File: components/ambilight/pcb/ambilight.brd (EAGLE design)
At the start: 69.2 x 54.7 mm, 12 parts, among them IC1 7805T

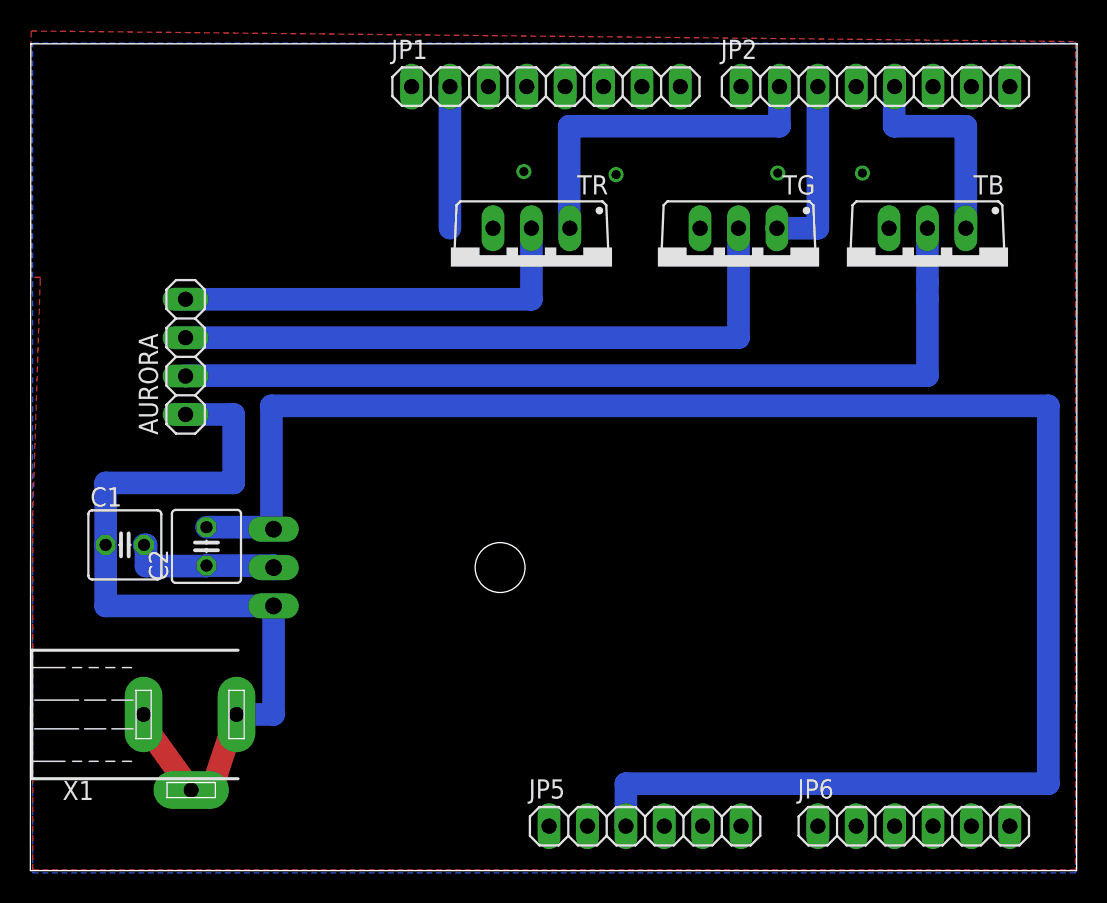
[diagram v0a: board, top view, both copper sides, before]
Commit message: Added Socket PCB, fixed ambilight sketch a bit
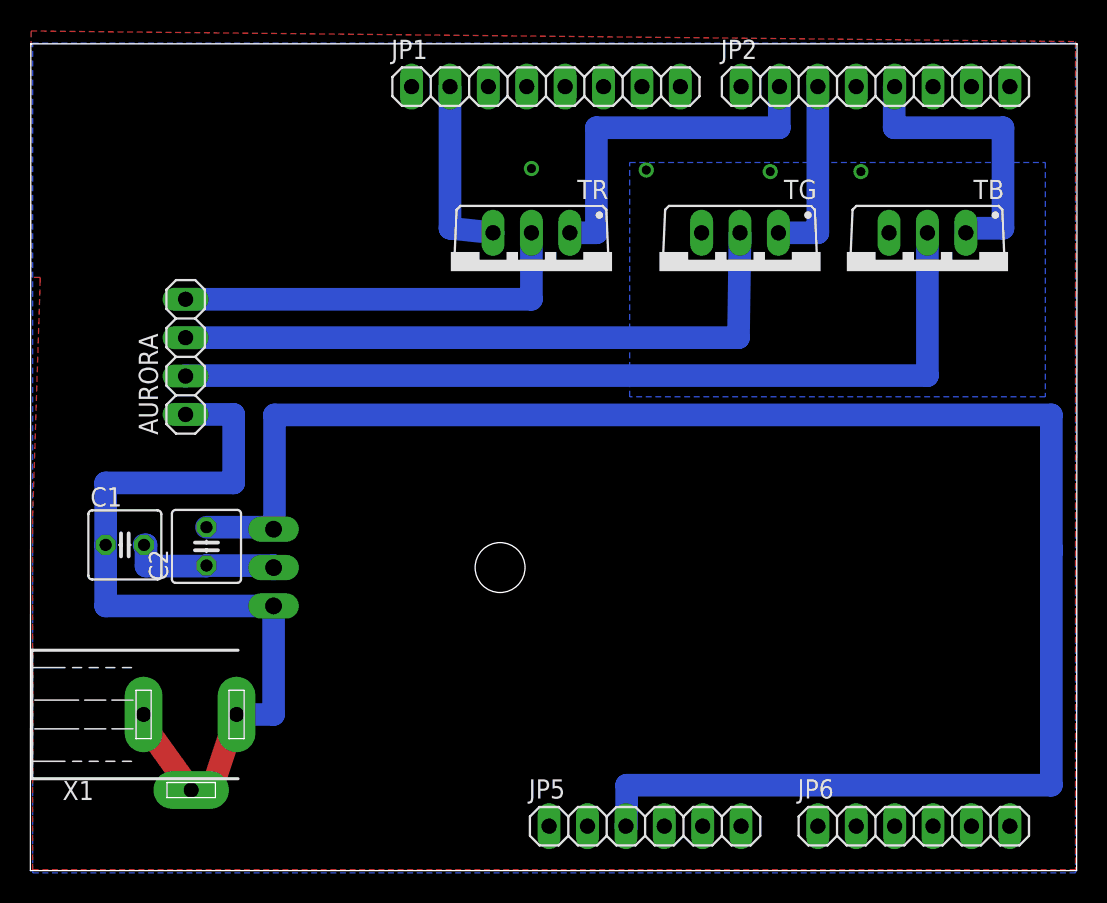
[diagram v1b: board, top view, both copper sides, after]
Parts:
- moved TG 0.32 mm to (77.4, 45.9)
- moved TB 0.30 mm to (89.8, 45.9)
- moved TR 0.30 mm to (63.6, 45.9)
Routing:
- net N$7: track 14.1 -> 19.4 mm
- net GND: track 25.3 -> 28.1 mm, vias 2 -> 4
- net N$4: track 120.0 -> 119.1 mm
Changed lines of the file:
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@@
 </autorouter>
 <elements>
-<element name="TR" library="transistor-power" package="TO220BV" value="foo" x="63.6" y="46.21" rot="R180"/>
-<element name="TG" library="transistor-power" package="TO220BV" value="foo" x="77.3" y="46.21" rot="R180"/>
-<element name="TB" library="transistor-power" package="TO220BV" value="foo" x="89.8" y="46.21" rot="R180"/>
+<element name="TR" library="transistor-power" package="TO220BV" value="foo" x="63.6" y="45.91" rot="R180"/>
+<element name="TG" library="transistor-power" package="TO220BV" value="foo" x="77.4" y="45.91" rot="R180"/>
+<element name="TB" library="transistor-power" package="TO220BV" value="foo" x="89.8" y="45.91" rot="R180"/>
 <element name="X1" library="con-conrad" package="733980-62" value="" x="35.52" y="16.58" rot="R270"/>
 <element name="AURORA" library="pinhead" package="1X04" value="" x="40.72" y="40.24" rot="R90"/>
@@
 <vertex x="30.5" y="61.8"/>
 </polygon>
-<via x="79.9" y="52.4" extent="1-16" drill="0.6" shape="square"/>
 <contactref element="JP1" pad="2"/>
-<wire x1="58.21" y1="48.75" x2="58.21" y2="58.12" width="1.5" layer="16"/>
-<via x="85.5" y="52.4" extent="1-16" drill="0.6" shape="square"/>
 <contactref element="X1" pad="2"/>
 <contactref element="X1" pad="3"/>
@@
 <wire x1="38.1" y1="26.4" x2="42.1" y2="26.4" width="1.5" layer="16"/>
 <wire x1="42.1" y1="26.4" x2="42.1" y2="26.43" width="1.5" layer="16"/>
+<wire x1="61.06" y1="48.45" x2="58.21" y2="48.75" width="1.5" layer="16"/>
+<wire x1="58.21" y1="48.75" x2="58.21" y2="58.12" width="1.5" layer="16"/>
+<polygon width="1.5" layer="16" spacing="1.2" isolate="0.8">
+<vertex x="70.1" y="53.1"/>
+<vertex x="97.6" y="53.1"/>
+<vertex x="97.6" y="37.6"/>
+<vertex x="70.1" y="37.6"/>
+</polygon>
+<via x="63.6" y="52.7" extent="1-16" drill="0.6"/>
+<via x="71.2" y="52.6" extent="1-16" drill="0.6"/>
+<via x="79.4" y="52.5" extent="1-16" drill="0.6"/>
+<via x="85.4" y="52.5" extent="1-16" drill="0.6"/>
 </signal>
 <signal name="N$4">
@@
 <contactref element="IC1" pad="3"/>
 <contactref element="C2" pad="2"/>
-<wire x1="46.54" y1="28.84" x2="46.4" y2="28.84" width="1.5" layer="16"/>
-<wire x1="46.4" y1="28.84" x2="46.4" y2="37" width="1.5" layer="16"/>
-<wire x1="46.4" y1="37" x2="97.8" y2="37" width="1.5" layer="16"/>
-<wire x1="97.8" y1="37" x2="97.8" y2="12" width="1.5" layer="16"/>
-<wire x1="97.8" y1="12" x2="69.85" y2="12" width="1.5" layer="16"/>
-<wire x1="69.85" y1="12" x2="69.85" y2="9.19" width="1.5" layer="16"/>
 <wire x1="42.1" y1="28.97" x2="46.54" y2="28.97" width="1.5" layer="16"/>
 <wire x1="46.54" y1="28.97" x2="46.54" y2="28.84" width="1.5" layer="16"/>
+<wire x1="46.54" y1="28.84" x2="46.4" y2="28.84" width="1.5" layer="16"/>
+<wire x1="46.54" y1="28.84" x2="46.6" y2="28.84" width="1.5" layer="16"/>
+<wire x1="46.6" y1="28.84" x2="46.6" y2="36.4" width="1.5" layer="16"/>
+<wire x1="46.6" y1="36.4" x2="98" y2="36.4" width="1.5" layer="16"/>
+<wire x1="98" y1="36.4" x2="98" y2="27.6" width="1.5" layer="16"/>
+<wire x1="98" y1="27.6" x2="98" y2="27.3" width="1.5" layer="16"/>
+<wire x1="69.85" y1="9.19" x2="69.9" y2="9.19" width="1.5" layer="16"/>
+<wire x1="69.9" y1="9.19" x2="69.9" y2="11.9" width="1.5" layer="16"/>
+<wire x1="69.9" y1="11.9" x2="98" y2="11.9" width="1.5" layer="16"/>
+<wire x1="98" y1="11.9" x2="98" y2="27.3" width="1.5" layer="16"/>
 </signal>
 <signal name="N$7">
@@
 <contactref element="JP2" pad="5"/>
 <wire x1="87.63" y1="58.12" x2="87.6" y2="58.12" width="1.5" layer="16"/>
-<wire x1="87.6" y1="58.12" x2="87.6" y2="55.5" width="1.5" layer="16"/>
-<wire x1="87.6" y1="55.5" x2="92.34" y2="55.5" width="1.5" layer="16"/>
-<wire x1="92.34" y1="55.5" x2="92.34" y2="48.75" width="1.5" layer="16"/>
+<wire x1="87.6" y1="58.12" x2="87.6" y2="55.4" width="1.5" layer="16"/>
+<wire x1="92.34" y1="48.45" x2="92.3" y2="48.75" width="1.5" layer="16"/>
+<wire x1="87.6" y1="55.4" x2="94.8" y2="55.4" width="1.5" layer="16"/>
+<wire x1="92.3" y1="48.75" x2="94.8" y2="48.75" width="1.5" layer="16"/>
+<wire x1="94.8" y1="48.75" x2="94.8" y2="55.4" width="1.5" layer="16"/>
 </signal>
 <signal name="N$9">
 <contactref element="TG" pad="G"/>
 <contactref element="JP2" pad="3"/>
-<wire x1="79.84" y1="48.75" x2="82.55" y2="48.75" width="1.5" layer="16"/>
-<wire x1="82.55" y1="48.75" x2="82.55" y2="58.12" width="1.5" layer="16"/>
+<wire x1="79.94" y1="48.45" x2="82.55" y2="48.45" width="1.5" layer="16"/>
+<wire x1="82.55" y1="48.45" x2="82.55" y2="58.12" width="1.5" layer="16"/>
 </signal>
 <signal name="N$10">
 <contactref element="TR" pad="G"/>
 <contactref element="JP2" pad="2"/>
-<wire x1="66.14" y1="48.75" x2="66.1" y2="48.75" width="1.5" layer="16"/>
-<wire x1="66.1" y1="48.75" x2="66.1" y2="55.5" width="1.5" layer="16"/>
-<wire x1="66.1" y1="55.5" x2="80.01" y2="55.5" width="1.5" layer="16"/>
-<wire x1="80.01" y1="55.5" x2="80.01" y2="58.12" width="1.5" layer="16"/>
+<wire x1="80.01" y1="58.12" x2="80" y2="58.12" width="1.5" layer="16"/>
+<wire x1="80" y1="58.12" x2="80" y2="55.4" width="1.5" layer="16"/>
+<wire x1="66.14" y1="48.45" x2="67.9" y2="48.45" width="1.5" layer="16"/>
+<wire x1="67.9" y1="48.45" x2="67.9" y2="55.4" width="1.5" layer="16"/>
+<wire x1="67.9" y1="55.4" x2="80" y2="55.4" width="1.5" layer="16"/>
 </signal>
 <signal name="N$11">
@@
 <contactref element="AURORA" pad="4"/>
 <wire x1="40.72" y1="44.05" x2="63.6" y2="44.05" width="1.5" layer="16"/>
-<wire x1="63.6" y1="44.05" x2="63.6" y2="48.75" width="1.5" layer="16"/>
+<wire x1="63.6" y1="44.05" x2="63.6" y2="48.45" width="1.5" layer="16"/>
 </signal>
 <signal name="N$12">
@@
 <contactref element="AURORA" pad="3"/>
 <wire x1="40.72" y1="41.51" x2="77.3" y2="41.51" width="1.5" layer="16"/>
-<wire x1="77.3" y1="41.51" x2="77.3" y2="48.75" width="1.5" layer="16"/>
+<wire x1="77.3" y1="41.51" x2="77.4" y2="48.45" width="1.5" layer="16"/>
 </signal>
 <signal name="N$13">
 <contactref element="TB" pad="D"/>
 <contactref element="AURORA" pad="2"/>
-<wire x1="89.8" y1="48.75" x2="89.8" y2="45.2" width="1.5" layer="16"/>
-<wire x1="89.8" y1="45.2" x2="89.8" y2="44.1" width="1.5" layer="16"/>
 <wire x1="89.8" y1="39" x2="40.72" y2="39" width="1.5" layer="16"/>
 <wire x1="40.72" y1="39" x2="40.72" y2="38.97" width="1.5" layer="16"/>
-<wire x1="89.8" y1="39" x2="89.8" y2="44.1" width="1.5" layer="16"/>
+<wire x1="89.8" y1="39" x2="89.8" y2="48.45" width="1.5" layer="16"/>
 </signal>
 <signal name="N$16">
@@
 </signal>
 <signal name="S$1">
-<via x="69.2" y="52.3" extent="1-16" drill="0.6" shape="square"/>
 </signal>
 <signal name="S$2">
-<via x="63.1" y="52.5" extent="1-16" drill="0.6" shape="square"/>
 </signal>
 </signals>

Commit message: Worked on pcbs
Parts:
- C1: device rcl:C025-050X050 -> resistor:C050-025X075
- moved C1 1.84 mm to (38.1, 29.0), turned to 270 degrees
- moved X1 0.22 mm to (35.7, 16.7)
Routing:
- net GND: track 28.1 -> 22.6 mm
- net S$3: track 0.00 -> 4.30 mm
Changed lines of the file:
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@@
 <element name="TG" library="transistor-power" package="TO220BV" value="foo" x="77.4" y="45.91" rot="R180"/>
 <element name="TB" library="transistor-power" package="TO220BV" value="foo" x="89.8" y="45.91" rot="R180"/>
-<element name="X1" library="con-conrad" package="733980-62" value="" x="35.52" y="16.58" rot="R270"/>
+<element name="X1" library="con-conrad" package="733980-62" value="" x="35.72" y="16.68" rot="R270"/>
 <element name="AURORA" library="pinhead" package="1X04" value="" x="40.72" y="40.24" rot="R90"/>
 <element name="JP1" library="pinhead" package="1X08" value="" x="64.56" y="58.12"/>
@@
 <element name="JP6" library="pinhead" package="1X06" value="" x="88.9" y="9.19"/>
 <element name="IC1" library="linear" package="TO220H" value="7805T" x="56.7" y="26.3" rot="MR90"/>
-<element name="C1" library="rcl" package="C025-050X050" value="330n" x="36.7" y="27.8"/>
+<element name="C1" library="resistor" package="C050-025X075" value="330n" x="38.1" y="29" rot="R270"/>
 <element name="C2" library="rcl" package="C025-050X050" value="100n" x="42.1" y="27.7" rot="R90"/>
 </elements>
@@
 <contactref element="C1" pad="2"/>
 <contactref element="C2" pad="1"/>
-<wire x1="41.09" y1="11.58" x2="37.78" y2="16.18" width="1.5" layer="1"/>
+<wire x1="41.29" y1="11.68" x2="37.78" y2="16.18" width="1.5" layer="1"/>
 <wire x1="46.54" y1="26.2" x2="46.54" y2="26.3" width="1.5" layer="16"/>
 <wire x1="42.1" y1="26.43" x2="46.54" y2="26.43" width="1.5" layer="16"/>
 <wire x1="46.54" y1="26.43" x2="46.54" y2="26.3" width="1.5" layer="16"/>
-<wire x1="37.97" y1="27.8" x2="38.1" y2="27.8" width="1.5" layer="16"/>
-<wire x1="38.1" y1="27.8" x2="38.1" y2="26.4" width="1.5" layer="16"/>
-<wire x1="38.1" y1="26.4" x2="42.1" y2="26.4" width="1.5" layer="16"/>
-<wire x1="42.1" y1="26.4" x2="42.1" y2="26.43" width="1.5" layer="16"/>
 <wire x1="61.06" y1="48.45" x2="58.21" y2="48.75" width="1.5" layer="16"/>
 <wire x1="58.21" y1="48.75" x2="58.21" y2="58.12" width="1.5" layer="16"/>
@@
 <contactref element="IC1" pad="1"/>
 <contactref element="C1" pad="1"/>
-<wire x1="44.09" y1="16.58" x2="42.3" y2="11.18" width="1.5" layer="1"/>
-<wire x1="44.09" y1="16.58" x2="46.54" y2="16.58" width="1.5" layer="16"/>
+<wire x1="44.29" y1="16.68" x2="42.3" y2="11.18" width="1.5" layer="1"/>
+<wire x1="44.29" y1="16.68" x2="46.54" y2="16.58" width="1.5" layer="16"/>
 <wire x1="46.54" y1="16.58" x2="46.54" y2="23.76" width="1.5" layer="16"/>
-<wire x1="40.72" y1="36.43" x2="43.9" y2="36.43" width="1.5" layer="16"/>
-<wire x1="43.9" y1="36.43" x2="43.9" y2="31.9" width="1.5" layer="16"/>
-<wire x1="35.43" y1="31.9" x2="35.43" y2="27.8" width="1.5" layer="16"/>
-<wire x1="46.54" y1="23.76" x2="35.43" y2="23.76" width="1.5" layer="16"/>
-<wire x1="35.43" y1="23.76" x2="35.43" y2="27.8" width="1.5" layer="16"/>
-<wire x1="43.9" y1="31.9" x2="35.43" y2="31.9" width="1.5" layer="16"/>
+<wire x1="38.1" y1="31.54" x2="44" y2="31.54" width="1.5" layer="16"/>
+<wire x1="44" y1="31.54" x2="44" y2="36.5" width="1.5" layer="16"/>
+<wire x1="44" y1="36.5" x2="40.72" y2="36.5" width="1.5" layer="16"/>
+<wire x1="40.72" y1="36.5" x2="40.72" y2="36.43" width="1.5" layer="16"/>
+<wire x1="46.54" y1="23.76" x2="35.4" y2="23.76" width="1.5" layer="16"/>
+<wire x1="35.4" y1="23.76" x2="35.4" y2="31.6" width="1.5" layer="16"/>
+<wire x1="35.4" y1="31.6" x2="37.7" y2="31.6" width="1.5" layer="16"/>
+<wire x1="37.7" y1="31.6" x2="38.1" y2="31.54" width="1.5" layer="16"/>
 </signal>
 <signal name="N$41">
@@
 <signal name="S$2">
 </signal>
+<signal name="S$3">
+<wire x1="38.5" y1="26.3" x2="42.1" y2="26.3" width="1.5" layer="16"/>
+<wire x1="42.1" y1="26.4" x2="42.1" y2="26.3" width="1.5" layer="16"/>
+<wire x1="38.5" y1="26.3" x2="37.9" y2="26.3" width="1.5" layer="16"/>
+</signal>
 </signals>
